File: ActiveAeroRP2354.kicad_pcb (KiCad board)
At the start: 4 copper layers, 30 x 80 mm, 72 parts, among them J1 TAGCONNECT, J2 Conn_01x04_MountingPin, J4 USB_C_Receptacle_USB2.0_16P, Q1 SiA449DJ, Q3 AO3401A, SW1 SW_Push, SW2 SW_Push, U1 RP2354A, U18 AP63205WU, U2 WE-TVS-82400102, U3 W25Q256JVS, U4 ADXL375, U5 MS5611-01BA, U6 SCH16T, U7 BMI563, U9 APS6404L-3SQRx-SN, Y1 ABM8-272-T3

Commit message: basic routing done
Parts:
- added BZ1: Buzzer, Buzzer_Beeper:Buzzer_CUI_CPT-9019S-SMT, F.Cu at (45.5, 80.8)
- added C26: 1uF, Capacitor_SMD:C_0402_1005Metric, B.Cu at (43.8, 91.8)
- added C27: 1uF, Capacitor_SMD:C_0402_1005Metric, B.Cu at (48.9, 92.7)
- added C28: 1uF, Capacitor_SMD:C_0402_1005Metric, B.Cu at (38.4, 91.8)
- added C29: 1uF, Capacitor_SMD:C_0402_1005Metric, B.Cu at (33.3, 91.9)
- added C30: 10uF, Capacitor_SMD:C_0402_1005Metric, B.Cu at (50.6, 48.6)
- added C31: 1uF, Capacitor_SMD:C_0402_1005Metric, B.Cu at (51.8, 45.6)
- added C43: 10nF, Capacitor_SMD:C_0402_1005Metric, B.Cu at (36.0, 43.7)
- added D6: PPS, LED_SMD:LED_0402_1005Metric, B.Cu at (48.9, 43.9)
- added FB2: LQG15HS47NJ02, Inductor_SMD:L_0402_1005Metric, B.Cu at (36.0, 47.5)
- added J10: UART1_RAD, Connector_JST:JST_GH_SM04B-GHS-TB_1x04-1MP_P1.25mm_Horizontal, B.Cu at (33.2, 59.2)
- added J12: SPI, Connector_JST:JST_GH_SM07B-GHS-TB_1x07-1MP_P1.25mm_Horizontal, B.Cu at (56.8, 65.1)
- added J3: SRV1, Connector_PinSocket_2.54mm:PinSocket_1x03_P2.54mm_Vertical, F.Cu at (41.4, 24.7)
- added J5: UFL, Connector_Coaxial:U.FL_Molex_MCRF_73412-0110_Vertical, B.Cu at (33.0, 45.8)
- added J6: ARM, Connector_JST:JST_XH_B2B-XH-AM_1x02_P2.50mm_Vertical, F.Cu at (57.1, 87.7)
- added J7: SRV2, Connector_PinSocket_2.54mm:PinSocket_1x03_P2.54mm_Vertical, F.Cu at (43.9, 24.7)
- added J8: SRV4, Connector_PinSocket_2.54mm:PinSocket_1x03_P2.54mm_Vertical, F.Cu at (49.0, 24.7)
- added J9: SRV3, Connector_PinSocket_2.54mm:PinSocket_1x03_P2.54mm_Vertical, F.Cu at (46.5, 24.7)
- added R16: 220, Resistor_SMD:R_0402_1005Metric, B.Cu at (44.5, 32.2)
- added R17: 220, Resistor_SMD:R_0402_1005Metric, B.Cu at (49.5, 32.1)
- added R18: 220, Resistor_SMD:R_0402_1005Metric, B.Cu at (46.8, 32.2)
- added R54: 10R 0.25W, Resistor_SMD:R_0402_1005Metric, B.Cu at (36.0, 45.6)
- added R56: 1k, Resistor_SMD:R_0402_1005Metric, B.Cu at (48.9, 45.8)
- added R7: 220, Resistor_SMD:R_0402_1005Metric, B.Cu at (41.9, 32.2)
- added U10: AP7347DQ-33W5-7, Package_TO_SOT_SMD:SOT-23-5, B.Cu at (46.4, 92.0)
- added U11: MAX-M10S, RF_GPS:ublox_MAX, B.Cu at (42.5, 44.5)
- added U12: MMC5983MA, Package_LGA:LGA-16_3x3mm_P0.5mm, B.Cu at (53.0, 47.8)
- added U8: AP7347DQ-11W5-7, Package_TO_SOT_SMD:SOT-23-5, B.Cu at (35.9, 92.2)
- BATT1: value AMASS_XT30 -> VBAT
- C1, C10, C11, C12, C13, C14, C15, C16, C17, C18, C19, C20, C21, C22, C24, C25, C3, C4, C47, C48, C5, C56, C6, C7, C8, C9, D1, D2, D3, J4, L4, Q1, Q3, R1, R10, R11, R12, R13, R14, R15, R2, R21, R22, R24, R3, R4, R49, R5, R6, R8, R9, SW1, SW2, U1, U18, U2, U3, U4, U5, U7, U9, Y1: moved to B.Cu
- C23: value 10uF -> 22uF; moved to B.Cu
- J1: value TAGCONNECT -> TGCNT
- J2: value Conn_01x04_MountingPin -> I2C; moved to B.Cu
- moved Q3 121.6 mm to (40.7, 88.2), turned to 90 degrees
- moved BATT1 113.5 mm to (43.9, 96.9)
- moved R6 111.1 mm to (39.9, 93.1), turned to 180 degrees
- moved R12 109.7 mm to (37.1, 68.2), turned to 90 degrees
- moved R13 109.2 mm to (37.1, 66.3), turned to -90 degrees
- moved C1 107.4 mm to (43.2, 88.6), turned to -90 degrees
- moved U7 107.0 mm to (51.1, 40.1), turned to 180 degrees
- moved R5 106.7 mm to (34.6, 42.0), turned to -90 degrees
- moved R1 106.1 mm to (39.5, 85.5)
- moved J2 105.8 mm to (33.3, 68.3), turned to 90 degrees
- moved C5 105.6 mm to (44.7, 88.6), turned to -90 degrees
- moved R2 104.2 mm to (39.5, 81.0)
- moved R49 103.8 mm to (50.0, 91.5), turned to 90 degrees
- moved R11 103.5 mm to (43.3, 65.9), turned to 90 degrees
- moved J1 102.8 mm to (33.5, 74.7)
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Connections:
- C2 pad 1: VBAT -> +8V4
- C23 pad 1: VBAT -> +8V4
- Q1 pad 1: VBAT -> Net-(J6-Pin_1)
- R9 pad 1: Net-(U1-RUN) -> /NRST
- U1 pad 10: unconnected-(U1-GPIO7-Pad10) -> /SRV_3
- U1 pad 12: unconnected-(U1-GPIO8-Pad12) -> /TX2
- U1 pad 13: unconnected-(U1-GPIO9-Pad13) -> /RX2
- U1 pad 14: unconnected-(U1-GPIO10-Pad14) -> /AC_INT1
- U1 pad 15: unconnected-(U1-GPIO11-Pad15) -> /AC_INT2
- U1 pad 16: unconnected-(U1-GPIO12-Pad16) -> /CS_ACCEL
- U1 pad 17: unconnected-(U1-GPIO13-Pad17) -> /CS_MAG
- U1 pad 18: unconnected-(U1-GPIO14-Pad18) -> /MAG_INT
- U1 pad 19: unconnected-(U1-GPIO15-Pad19) -> /BZ
- U1 pad 2: unconnected-(U1-GPIO0-Pad2) -> /GPIO0
- U1 pad 26: Net-(U1-RUN) -> /NRST
- U1 pad 27: unconnected-(U1-GPIO16-Pad27) -> /NEOPIX
- U1 pad 28: unconnected-(U1-GPIO17-Pad28) -> /IMU1_INT1
- U1 pad 29: unconnected-(U1-GPIO18-Pad29) -> /IMU1_CS
- U1 pad 3: unconnected-(U1-GPIO1-Pad3) -> /CS1
- U1 pad 31: unconnected-(U1-GPIO19-Pad31) -> /SDA
- U1 pad 32: unconnected-(U1-GPIO20-Pad32) -> /SCL
- U1 pad 33: unconnected-(U1-GPIO21-Pad33) -> /TX1
- U1 pad 34: unconnected-(U1-GPIO22-Pad34) -> /RX1
- U1 pad 35: unconnected-(U1-GPIO23-Pad35) -> /CS_BARO
- U1 pad 36: unconnected-(U1-GPIO24-Pad36) -> /IMU_CS
- U1 pad 37: unconnected-(U1-GPIO25-Pad37) -> /IMU_RST
- U1 pad 4: unconnected-(U1-GPIO2-Pad4) -> /CS2
- U1 pad 40: unconnected-(U1-GPIO26/ADC0-Pad40) -> /VINSENSE
- U1 pad 41: unconnected-(U1-GPIO27/ADC1-Pad41) -> /IMU_INT
- U1 pad 42: unconnected-(U1-GPIO28/ADC2-Pad42) -> /SRV_2
- U1 pad 43: unconnected-(U1-GPIO29/ADC3-Pad43) -> /SRV_1
- U1 pad 5: unconnected-(U1-GPIO3-Pad5) -> /MOSI
- U1 pad 7: unconnected-(U1-GPIO4-Pad7) -> /MISO
- U1 pad 8: unconnected-(U1-GPIO5-Pad8) -> /SCK
- U1 pad 9: unconnected-(U1-GPIO6-Pad9) -> /SRV_4
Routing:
- net +5V: track 0.00 -> 124.2 mm
- net /SCK: track 0.00 -> 85.4 mm, vias 0 -> 7
- net /MISO: track 0.00 -> 80.9 mm, vias 0 -> 6
- net +8V4: track 0.00 -> 78.0 mm, vias 0 -> 8
- net /MOSI: track 0.00 -> 74.3 mm, vias 0 -> 5
- net +3V3: track 0.00 -> 57.5 mm, vias 0 -> 32
- net /NEOPIX: track 0.00 -> 56.7 mm, vias 0 -> 3
- net /NRST: track 0.00 -> 53.5 mm, vias 0 -> 2
- net /IMU_CS: track 0.00 -> 52.2 mm, vias 0 -> 3
- net +1V1: track 0.00 -> 46.8 mm, vias 0 -> 4
- net /IMU_RST: track 0.00 -> 46.6 mm, vias 0 -> 3
- net /IMU1_CS: track 0.00 -> 46.0 mm, vias 0 -> 3
- net /SRV_3: track 0.00 -> 44.9 mm, vias 0 -> 2
- net /AC_INT2: track 0.00 -> 44.6 mm, vias 0 -> 2
- net /SRV_4: track 0.00 -> 44.4 mm, vias 0 -> 2
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- added copper zone on In1.Cu, net +3V3
- added copper zone on B.Cu, net +8V4
- added copper zone on B.Cu, net GND
- added copper zone on F.Cu, net GND
- added copper zone on In2.Cu, net GND
- added copper zone on B.Cu, net Net-(J6-Pin_1)
- added copper zone on F.Cu, net VBAT
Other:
- board size 30 x 80 mm -> 30 x 77 mm
- board text added: "1 2 3 4"
- board text added: "2S LiPo"
- board text added: "A"
- board text added: "ARM + -"
- board text added: "B"
- board text added: "BOOT"
- board text added: "G 8V S"
- board text added: "GNSS L1"
- board text added: "I2C"
- board text added: "RADIO"
- board text added: "RST"
- board text added: "SCH16T-K01"
- board text added: "SPI EXP"
- board text added: "USB-C"

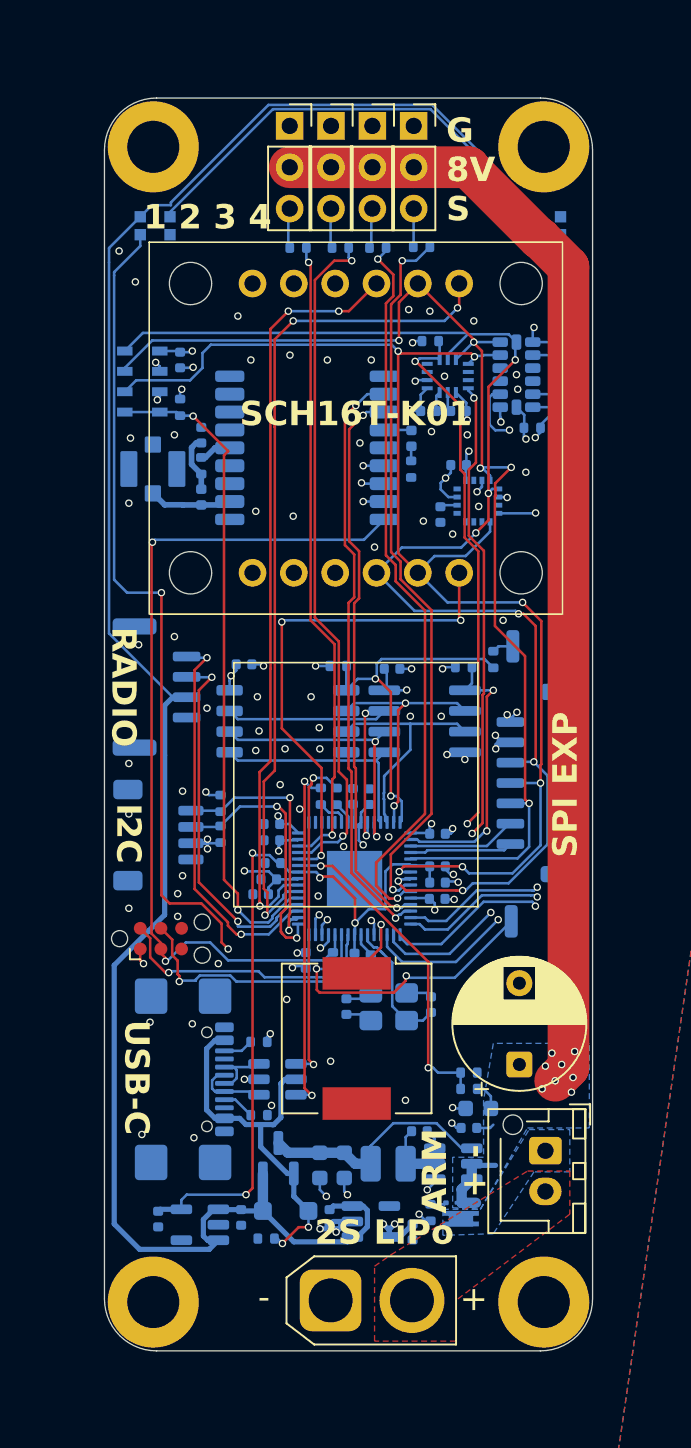
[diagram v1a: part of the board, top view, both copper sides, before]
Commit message: switched to double sided stm32h747xi
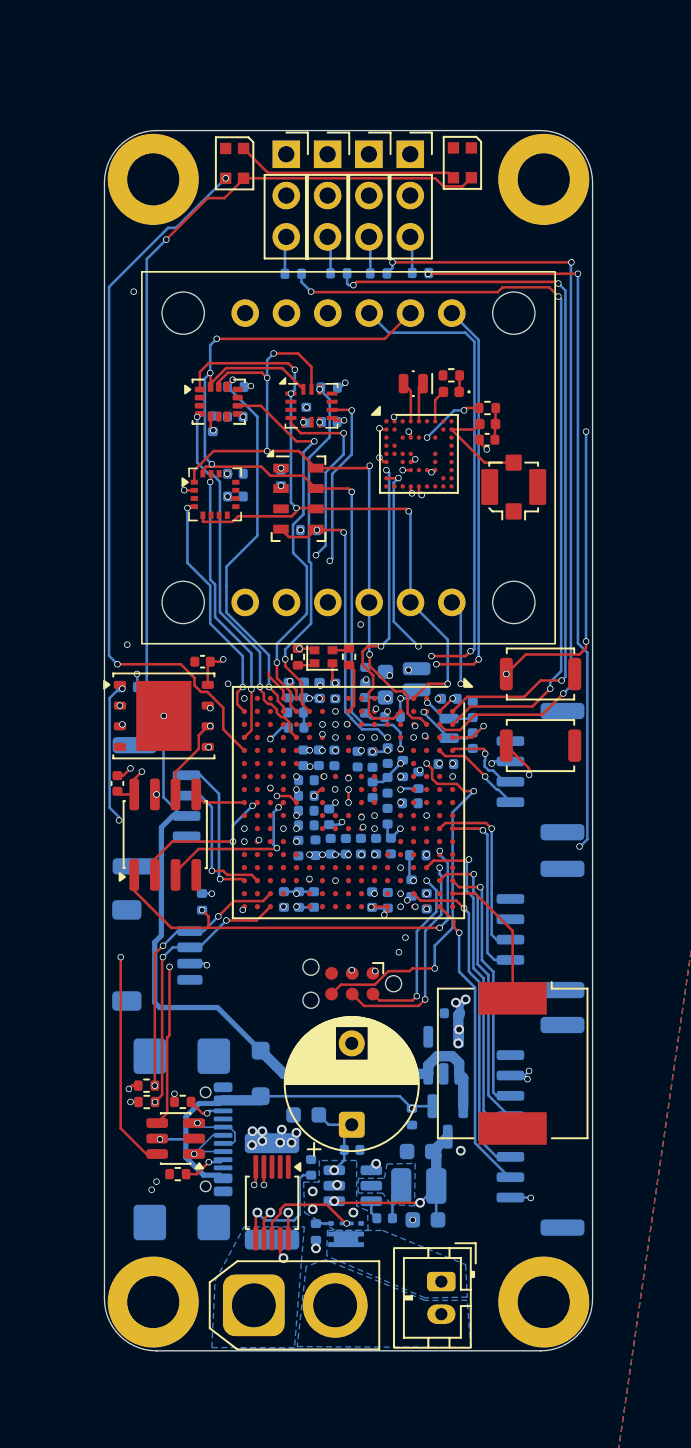
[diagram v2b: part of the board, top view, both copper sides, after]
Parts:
- removed R11, R15: 27, Resistor_SMD:R_0402_1005Metric
- removed R21: 180k, Resistor_SMD:R_0402_1005Metric
- removed R22: 56k, Resistor_SMD:R_0402_1005Metric
- removed U11: MAX-M10S, RF_GPS:ublox_MAX
- added C32: 100nF, Capacitor_SMD:C_0402_1005Metric, B.Cu at (44.1, 63.6)
- added C33: 100nF, Capacitor_SMD:C_0402_1005Metric, B.Cu at (42.2, 63.5)
- added C34: 100nF, Capacitor_SMD:C_0402_1005Metric, B.Cu at (43.0, 69.1)
- added C35: 100nF, Capacitor_SMD:C_0402_1005Metric, B.Cu at (48.8, 66.3)
- added C36: 100nF, Capacitor_SMD:C_0402_1005Metric, B.Cu at (46.5, 65.5)
- added C37: 100nF, Capacitor_SMD:C_0402_1005Metric, B.Cu at (43.2, 63.5)
- added C38: 100nF, Capacitor_SMD:C_0402_1005Metric, B.Cu at (42.4, 66.8)
- added C39: 100nF, Capacitor_SMD:C_0402_1005Metric, B.Cu at (42.4, 67.7)
- added C40: 100nF, Capacitor_SMD:C_0402_1005Metric, B.Cu at (41.9, 69.1)
- added C41: 100nF, Capacitor_SMD:C_0402_1005Metric, B.Cu at (45.6, 63.6)
- added C42: 100nF, Capacitor_SMD:C_0402_1005Metric, B.Cu at (42.4, 64.9)
- added C44: 100nF, Capacitor_SMD:C_0402_1005Metric, B.Cu at (42.4, 65.9)
- added C45: 100nF, Capacitor_SMD:C_0402_1005Metric, B.Cu at (47.4, 72.3)
- added C46: 100nF, Capacitor_SMD:C_0402_1005Metric, B.Cu at (46.5, 72.3)
- added C49: 1uF, Capacitor_SMD:C_0402_1005Metric, B.Cu at (41.0, 72.3)
- added C50: 100nF, Capacitor_SMD:C_0402_1005Metric, B.Cu at (42.0, 72.3)
- added C51: 2.2uF, Capacitor_SMD:C_0402_1005Metric, B.Cu at (42.9, 72.3)
- added C52: 4.7uF, Capacitor_SMD:C_0402_1005Metric, B.Cu at (51.0, 63.9)
- added C53: 4.7uF, Capacitor_SMD:C_0402_1005Metric, B.Cu at (49.8, 72.4)
- added C54: 10uF, Capacitor_SMD:C_0402_1005Metric, B.Cu at (46.0, 58.5)
- added C55: 10uF, Capacitor_SMD:C_0402_1005Metric, B.Cu at (46.0, 60.3)
- added C57: 220pF, Capacitor_SMD:C_0402_1005Metric, B.Cu at (47.7, 61.0)
- added C58: 100nF, Capacitor_SMD:C_0402_1005Metric, B.Cu at (44.2, 59.4)
- added C59: 100nF, Capacitor_SMD:C_0402_1005Metric, B.Cu at (42.7, 88.7)
- added FB1: FCM1608KF-601T03, Inductor_SMD:L_0402_1005Metric, B.Cu at (43.2, 59.4)
- added FB3: LSMCA160808T180NGR, Inductor_SMD:L_0603_1608Metric, B.Cu at (47.3, 59.1)
- added J11: SPI, Connector_JST:JST_GH_SM08B-GHS-TB_1x08-1MP_P1.25mm_Horizontal, B.Cu at (56.8, 86.2)
- added J13: RUNCAM, Connector_JST:JST_GH_SM04B-GHS-TB_1x04-1MP_P1.25mm_Horizontal, B.Cu at (56.8, 74.1)
- added L1: L_Small, Inductor_SMD:L_Changjiang_FTC201607S, B.Cu at (49.2, 58.7)
- added R19: 10k, Resistor_SMD:R_0402_1005Metric, B.Cu at (38.1, 40.7)
- added R20: 51, Resistor_SMD:R_0402_1005Metric, F.Cu at (45.0, 57.3)
- added R23: 10k, Resistor_SMD:R_0402_1005Metric, B.Cu at (48.9, 71.6)
- added R25: 10k, Resistor_SMD:R_0402_1005Metric, B.Cu at (49.3, 69.5)
- added U13: STM32H747XIHx, Package_BGA:TFBGA-265_14x14mm_Layout17x17_P0.8mm, F.Cu at (45.0, 66.3)
- added Y2: 32.768khz, Crystal:Crystal_SMD_MicroCrystal_CM9V-T1A-2Pin_1.6x1.0mm, F.Cu at (49.0, 40.6)
- added Y3: 25Mhz, Oscillator:Oscillator_SMD_Abracon_ASCO-4Pin_1.6x1.2mm, F.Cu at (43.5, 57.3)
- C10, C11: value 15pF -> 100nF
- C19: value 10uF -> 100nF
- C22, C25: value 4.7uF -> 1uF
- C28, C29: value 1uF -> 8pF
- C3, C43, C6, D2, D3, D6, FB2, J5, R1, R12, R13, R2, R54, R56, SW1, SW2, U12, U2, U5, U7, U9: moved to F.Cu
- C7: value 0.1uF -> 100nF
- C8: value 1uF -> 100nF
- J12: value SPI -> UART3; footprint Connector_JST:JST_GH_SM07B-GHS-TB_1x07-1MP_P1.25mm_Horizontal -> Connector_JST:JST_GH_SM04B-GHS-TB_1x04-1MP_P1.25mm_Horizontal
- J6: footprint Connector_JST:JST_XH_B2B-XH-AM_1x02_P2.50mm_Vertical -> Connector_JST:JST_PH_B2B-PH-K_1x02_P2.00mm_Vertical
- R10: value 1k -> 10k; moved to F.Cu
- R9: value 1k -> 0.01R; footprint Resistor_SMD:R_0402_1005Metric -> Resistor_SMD:R_2512_6332Metric
- U1: value RP2354A -> LSM6DSV320; footprint Package_DFN_QFN:QFN-60-1EP_7x7mm_P0.4mm_EP3.4x3.4mm -> Package_LGA:LGA-14_3x2.5mm_P0.5mm_LayoutBorder3x4y; moved to F.Cu
- U3: value W25Q256JVS -> MIA-M10Q; footprint Package_SO:SOIC-8_5.3x5.3mm_P1.27mm -> Package_LGA:ublox_LGA-53_4.5x4.5mm_Layout9x9_P0.5mm; moved to F.Cu
- U4: value ADXL375 -> W25N512GV; footprint Package_LGA:LGA-14_3x5mm_P0.8mm_LayoutBorder1x6y -> Package_SON:WSON-8-1EP_6x5mm_P1.27mm_EP3.4x4.3mm; moved to F.Cu
- U8: value AP7347DQ-11W5-7 -> INA238; footprint Package_TO_SOT_SMD:SOT-23-5 -> Package_SO:VSSOP-10_3x3mm_P0.5mm; moved to F.Cu
- Y1: value ABM8-272-T3 -> ECS-.327-6-1210-TR; footprint Crystal:Crystal_SMD_3225-4Pin_3.2x2.5mm -> Crystal:Crystal_SMD_MicroCrystal_CM9V-T1A-2Pin_1.6x1.0mm
- moved C29 36.8 mm to (52.6, 60.6), turned to 90 degrees
- moved C28 32.6 mm to (52.6, 62.5)
- moved U1 30.5 mm to (37.0, 41.7), turned to 0 degrees
- moved U4 30.2 mm to (33.6, 61.0), turned to 0 degrees
- moved H3 24.0 mm to (57.0, 97.0)
- moved H4 24.0 mm to (33.0, 97.0)
- moved R4 22.4 mm to (48.3, 64.2), turned to 90 degrees
- moved J5 22.2 mm to (55.2, 46.9)
- moved R14 21.6 mm to (36.0, 72.4), turned to -90 degrees
- moved C8 21.0 mm to (36.7, 43.0)
- moved C7 20.0 mm to (38.0, 42.6), turned to 0 degrees
- moved R10 19.3 mm to (41.9, 57.4), turned to 90 degrees
- moved U3 18.3 mm to (49.3, 44.9), turned to 0 degrees
- moved C6 18.3 mm to (30.8, 65.1), turned to 90 degrees
- moved FB2 18.2 mm to (53.6, 43.0), turned to 0 degrees
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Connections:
- BATT1 pad 1: GND -> /MON_GND
- C10 pad 1: GND -> +3V3
- C10 pad 2: Net-(U1-XIN) -> GND
- C11 pad 1: GND -> +3V3
- C11 pad 2: Net-(C11-Pad2) -> GND
- C20 pad 1: GND -> /VDDA
- C20 pad 2: +1V1 -> GND
- C21 pad 1: +1V1 -> /VDDA
- C22 pad 1: +1V1 -> /VDDA
- C25 pad 1: +1V1 -> /VDDA
- C28 pad 1: +5V -> Net-(U13-PC14)
- C29 pad 1: +1V1 -> Net-(U13-PC15)
- J1 pad 6: unconnected-(J1-SWO-Pad6) -> /SWO
- J12 pad 3: /SCK -> /RX3
- J12 pad 4: /MISO -> /TX3
- R10 pad 1: Net-(U1-XOUT) -> Net-(Y3-Tri-State)
- R10 pad 2: Net-(C11-Pad2) -> +3V3
- R14 pad 2: /GPIO0 -> /PSRAM_CS
- R3 pad 2: /QSPI_SS -> /FLASH_CS
- R4 pad 1: +3V3 -> Net-(U13-PDR_ON)
- R4 pad 2: /CS_ACCEL -> +3V3
- R54 pad 1: Net-(U11-VCC_RF) -> Net-(U3-VCC_RF)
- R8 pad 1: /QSPI_SS -> Net-(U13-BOOT0)
- R9 pad 1: /NRST -> GND
- R9 pad 2: Net-(R9-Pad2) -> /MON_GND
- SW2 pad 1: Net-(R9-Pad2) -> /NRST
- U1 pad 1: +3V3 -> /MISO
- U1 pad 10: /SRV_3 -> unconnected-(U1-NC-Pad10)
- U1 pad 11: +3V3 -> unconnected-(U1-NC-Pad11)
- U1 pad 12: /TX2 -> /CS_ACCEL
- U1 pad 13: /RX2 -> /SCK
- U1 pad 14: /AC_INT1 -> /MOSI
- U1 pad 2: /GPIO0 -> unconnected-(U1-SDX-Pad2)
- U1 pad 3: /CS1 -> unconnected-(U1-SCX-Pad3)
- U1 pad 4: /CS2 -> /AC_INT1
- U1 pad 5: /MOSI -> +3V3
- U1 pad 6: +1V1 -> GND
- U1 pad 7: /MISO -> GND
- U1 pad 8: /SCK -> +3V3
- U1 pad 9: /SRV_4 -> /AC_INT2
- U2 pad 4: Net-(R15-Pad2) -> /USB_D+
- U2 pad 6: Net-(R11-Pad2) -> /USB_D-
- U4 pad 1: +3V3 -> /FLASH_CS
- U4 pad 2: GND -> /FLASH_SD1
- U4 pad 3: unconnected-(U4-RES-Pad3) -> /FLASH_SD2
- U4 pad 5: GND -> /FLASH_SD0
- U4 pad 6: +3V3 -> /QSPI_SCK
- U4 pad 7: /CS_ACCEL -> /FLASH_SD3
- U4 pad 8: /AC_INT1 -> +3V3
- U4 pad 9: /AC_INT2 -> GND
- U8 pad 1: +5V -> GND
- U8 pad 3: +5V -> unconnected-(U8-~{Alert}-Pad3)
- U8 pad 4: unconnected-(U8-NC-Pad4) -> /SCL
- U8 pad 5: +1V1 -> /SDA
- U9 pad 1: /GPIO0 -> /PSRAM_CS
- U9 pad 2: /QSPI_SD1 -> /PSRAM_SD1
- U9 pad 3: /QSPI_SD2 -> /PSRAM_SD2
- U9 pad 5: /QSPI_SD0 -> /PSRAM_SD0
- U9 pad 7: /QSPI_SD3 -> /PSRAM_SD3
- Y1 pad 1: Net-(U1-XIN) -> Net-(U13-PC15)
- Y1 pad 2: GND -> Net-(U13-PC14)
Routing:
- net +8V4: track 78.0 -> 13.5 mm, vias 8 -> 7
- net +1V1: track 46.8 -> 0.00 mm, vias 4 -> 0
- net /VDDSDC: track 0.00 -> 42.8 mm, vias 0 -> 10
- net /SCK: track 85.4 -> 44.3 mm, vias 7 -> 5
- net /MISO: track 80.9 -> 43.7 mm, vias 6 -> 5
- net /USB_D-: track 1.96 -> 33.4 mm, vias 0 -> 3
- net +5V: track 124.2 -> 94.9 mm, vias 0 -> 1
- net /PSRAM_CS: track 0.00 -> 27.3 mm, vias 0 -> 3
- net /USB_D+: track 1.38 -> 28.3 mm, vias 0 -> 3
- net /MAG_INT: track 43.8 -> 17.5 mm
- net /IMU1_CS: track 46.0 -> 22.0 mm, vias 3 -> 2
- net /IMU1_INT2: track 0.76 -> 24.0 mm, vias 1 -> 3
- net /SWO: track 0.00 -> 22.9 mm, vias 0 -> 3
- net /CS_MAG: track 37.6 -> 14.7 mm
- net /CS_BARO: track 40.7 -> 18.7 mm, vias 2 -> 3
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- added copper zone on In4.Cu, net +3V3
- added copper zone on In2.Cu, net +8V4
- added copper zone on B.Cu, net /MON_GND
- added copper zone on In1.Cu, net GND
- added copper zone on In3.Cu, net GND
- added copper zone on B.Cu, net Net-(U18-SW)
- added copper zone on B.Cu, net VBAT
- removed copper zone on In1.Cu, net +3V3
- removed copper zone on In2.Cu, net GND
- removed copper zone on F.Cu, net VBAT
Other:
- board size 30 x 77 mm -> 30 x 75 mm
- copper layers 4 -> 6
- board text removed: "1 2 3 4"
- board text removed: "2S LiPo"
- board text removed: "A"
- board text removed: "ARM + -"
- board text removed: "B"
- board text removed: "BOOT"
- board text removed: "G 8V S"
- board text removed: "GNSS L1"
- board text removed: "I2C"
- board text removed: "RADIO"
- board text removed: "RST"
- board text removed: "SCH16T-K01"
- board text removed: "SPI EXP"
- board text removed: "USB-C"

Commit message: design lock (probably), added silks
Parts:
- added C60: 100nF, Capacitor_SMD:C_0402_1005Metric, B.Cu at (40.5, 64.9)
- added C61: 100nF, Capacitor_SMD:C_0402_1005Metric, B.Cu at (39.8, 60.1)
- added C62: 4.7uF, Capacitor_SMD:C_0402_1005Metric, B.Cu at (36.9, 67.5)
- added C63: 100pF, Capacitor_SMD:C_0402_1005Metric, B.Cu at (35.9, 70.5)
- added C64: 100pF, Capacitor_SMD:C_0402_1005Metric, B.Cu at (35.9, 64.5)
- added D4: ESD2CANFD24, Package_TO_SOT_SMD:SOT-23-3, B.Cu at (39.5, 67.1)
- added J14: Conn_01x06_MountingPin, Connector_JST:JST_GH_SM06B-GHS-TB_1x06-1MP_P1.25mm_Horizontal, B.Cu at (56.8, 45.1)
- added J15: Conn_01x03_MountingPin, Connector_JST:JST_GH_SM03B-GHS-TB_1x03-1MP_P1.25mm_Horizontal, B.Cu at (33.2, 67.5)
- added L2: DLW32SH101XF2L, FCU2025Lib:FIL_DLW32SH101XF2L, B.Cu at (34.8, 61.0)
- added Q2: AO3401A, Package_TO_SOT_SMD:SOT-23, F.Cu at (57.6, 73.8)
- added R11: 220, Resistor_SMD:R_0402_1005Metric, F.Cu at (58.2, 76.5)
- added R15: 10k, Resistor_SMD:R_0402_1005Metric, F.Cu at (59.2, 76.5)
- added R21: 10k, Resistor_SMD:R_0402_1005Metric, B.Cu at (37.6, 75.3)
- added R22: 10k, Resistor_SMD:R_0402_1005Metric, B.Cu at (37.6, 76.3)
- added R26: 60R, Resistor_SMD:R_0402_1005Metric, B.Cu at (36.9, 69.4)
- added R27: 60R, Resistor_SMD:R_0402_1005Metric, B.Cu at (36.9, 65.7)
- added REF**: Untitled, FCU2025Lib:Untitled, F.Cu at (56.1, 42.4)
- added U11: MCP2562-E-MF, Package_DFN_QFN:DFN-8-1EP_3x3mm_P0.65mm_EP1.55x2.4mm, B.Cu at (38.2, 62.6)
- R12, R13: moved to B.Cu
- moved J10 21.4 mm to (33.2, 45.1)
- moved R12 9.19 mm to (38.3, 77.5)
- moved R13 7.73 mm to (38.3, 78.5)
- moved SW1 3.20 mm to (56.9, 66.0)
- moved C48 2.67 mm to (41.8, 41.2), turned to 0 degrees
- moved C31 2.52 mm to (38.7, 48.5), turned to 90 degrees
- moved R24 2.09 mm to (43.2, 42.8), turned to 90 degrees
- moved C8 1.80 mm to (36.1, 41.3)
- moved C30 1.75 mm to (37.2, 49.0), turned to 90 degrees
- moved C47 1.11 mm to (41.3, 42.6)
- moved U12 0.68 mm to (37.5, 47.2), turned to -90 degrees
- moved U7 0.59 mm to (42.1, 41.8), turned to -90 degrees
- moved J1 0.30 mm to (45.0, 77.2)
- moved SW2 0.10 mm to (56.9, 58.4)
- moved C7 0.08 mm to (38.1, 42.6)
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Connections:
- J13 pad 2: unconnected-(J13-Pin_2-Pad2) -> Net-(J13-Pin_2)
- J2 pad 3: /SDA -> /SDA1
- J2 pad 4: /SCL -> /SCL1
- U13 pad A10: unconnected-(U13-PG9-PadA10) -> /RX5
- U13 pad A14: unconnected-(U13-PA15-PadA14) -> /CAM_SW
- U13 pad B10: unconnected-(U13-PJ15-PadB10) -> /GPS_RST
- U13 pad C11: unconnected-(U13-PD7-PadC11) -> /GPS_INT
- U13 pad C9: unconnected-(U13-PG12-PadC9) -> /RTS5
- U13 pad D6: unconnected-(U13-PG15-PadD6) -> /TX5
- U13 pad D8: unconnected-(U13-PG14-PadD8) -> /CTS5
- U13 pad P16: unconnected-(U13-PD14-PadP16) -> /ALRT
- U13 pad P5: unconnected-(U13-PI15-PadP5) -> /CAN_SHDN
- U13 pad T13: unconnected-(U13-PH8-PadT13) -> /SDA1
- U13 pad T14: unconnected-(U13-PB12-PadT14) -> /CAN_RX
- U13 pad U13: unconnected-(U13-PH7-PadU13) -> /SCL1
- U13 pad U14: unconnected-(U13-PB13-PadU14) -> /CAN_TX
- U3 pad A6: unconnected-(U3-EXTINT-PadA6) -> /GPS_INT
- U3 pad C4: /NRST -> /GPS_RST
- U8 pad 3: unconnected-(U8-~{Alert}-Pad3) -> /ALRT
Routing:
- net /GPS_INT: track 0.00 -> 45.4 mm, vias 0 -> 5
- net /GPS_RST: track 0.00 -> 44.6 mm, vias 0 -> 5
- net /CTS5: track 0.00 -> 32.9 mm, vias 0 -> 2
- net /TX5: track 0.00 -> 31.4 mm, vias 0 -> 3
- net /RX5: track 0.00 -> 31.4 mm, vias 0 -> 2
- net /NRST: track 60.5 -> 30.4 mm, vias 6 -> 3
- net /RTS5: track 0.00 -> 28.7 mm, vias 0 -> 3
- net +5V: track 94.9 -> 122.1 mm, vias 1 -> 4
- net /TX1: track 9.26 -> 30.5 mm, vias 1 -> 2
- net /RX1: track 8.81 -> 29.0 mm, vias 1 -> 2
- net /ALRT: track 0.00 -> 19.5 mm, vias 0 -> 3
- net /CAN_TX: track 0.00 -> 13.7 mm, vias 0 -> 2
- net /CAM_SW: track 0.00 -> 13.4 mm
- net Net-(J15-Pin_1): track 0.00 -> 12.8 mm
- net GND: track 34.1 -> 46.4 mm, vias 59 -> 185
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- added copper zone on F.Cu, net +8V4
- added copper zone on B.Cu, net Net-(J13-Pin_2)
- added copper zone on F.Cu, net Net-(J13-Pin_2)
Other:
- board text added: "-"
- board text added: "- +"
- board text added: "2S LiPo"
- board text added: "A B C D"
- board text added: "ARM"
- board text added: "BARO"
- board text added: "BOOT"
- board text added: "CAN"
- board text added: "G 8V S"
- board text added: "HI-G"
- board text added: "I2C"
- board text added: "IMU"
- board text added: "L"
- board text added: "L1 GNSS"
- board text added: "MAG"
- board text added: "R"
- board text added: "RST"
- board text added: "SCH16T-K01"
- board text added: "SENSORS"
- board text added: "SPI EXP"
- board text added: "STM32H747XI"
- board text added: "UART1 5V"
- board text added: "UART3"
- board text added: "UART4 8V"
- board text added: "UART5 SiK 5V"

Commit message: cleaned up silkscreens and layout
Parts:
- added G***: LOGO, LOGO, F.Cu at (35.2, 77.2)
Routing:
- net GND: track 46.4 -> 51.2 mm, vias 185 -> 200
- net /ALRT: track 19.5 -> 17.6 mm
- net /IMU1_INT1: track 28.9 -> 28.3 mm, vias 4 -> 3
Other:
- board text added: "FLASH"
- board text added: "H747XI"
- board text added: "PSRAM"
- board text added: "SCH16T"
- board text added: "USB-C"
- board text added: "VENUS"
- board text added: "Venus FC v1.0 Kaiwen Zheng 2026 Leviathan Flight Systems"
- board text removed: "SCH16T-K01"
- board text removed: "STM32H747XI"
